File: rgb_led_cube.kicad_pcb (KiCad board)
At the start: 2 copper layers, 246.4 x 238.8 mm, 90 parts, among them Q1 IRLML6401TRPBF, Q10 MMBT2222A-TP, Q11 IRLML6401TRPBF, Q12 MMBT2222A-TP, Q13 IRLML6401TRPBF, Q14 MMBT2222A-TP, Q15 IRLML6401TRPBF, Q16 MMBT2222A-TP, Q2 MMBT2222A-TP, Q3 IRLML6401TRPBF, Q4 MMBT2222A-TP, Q5 IRLML6401TRPBF, Q6 MMBT2222A-TP, Q7 IRLML6401TRPBF, Q8 MMBT2222A-TP, Q9 IRLML6401TRPBF, U1 TLC59711PWPR, U10 TLC59711PWPR, U11 TLC59711PWPR, U12 TLC59711PWPR, U13 TLC59711PWPR, U14 TLC59711PWPR, U15 TLC59711PWPR, U16 TLC59711PWPR, U2 TLC59711PWPR, U3 TLC59711PWPR, U4 TLC59711PWPR, U5 TLC59711PWPR, U6 TLC59711PWPR, U7 TLC59711PWPR, U8 TLC59711PWPR, U9 TLC59711PWPR

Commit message: Add microphone
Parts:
- added C17: 0.1µF, Capacitor_SMD:C_0805_2012Metric_Pad1.15x1.40mm_HandSolder, F.Cu at (155.8, 70.7)
- added MK1: ICS-43434, rgb_led_cube:MIC_ICS-43434, F.Cu at (151.1, 69.6)
- added R41: 100K, Resistor_SMD:R_0805_2012Metric_Pad1.15x1.40mm_HandSolder, F.Cu at (155.8, 68.5)
- added REF1: MountingHole_3.2mm_M3, MountingHole:MountingHole_3.2mm_M3, F.Cu at (31.4, 27.4)
- added REF2: MountingHole_3.2mm_M3, MountingHole:MountingHole_3.2mm_M3, F.Cu at (269.4, 27.4)
- added REF3: MountingHole_3.2mm_M3, MountingHole:MountingHole_3.2mm_M3, F.Cu at (269.4, 265.4)
- added REF4: MountingHole_3.2mm_M3, MountingHole:MountingHole_3.2mm_M3, F.Cu at (31.4, 265.4)
- moved CNTL1 102.8 mm to (150.4, 70.3)
- moved U11 18.7 mm to (94.6, 173.8)
- moved U13 18.7 mm to (94.6, 201.7)
- moved U15 18.7 mm to (94.6, 229.6)
- moved U7 18.7 mm to (94.6, 117.9)
- moved U9 18.7 mm to (94.6, 145.8)
- moved U10 18.7 mm to (206.4, 145.8)
- moved U12 18.7 mm to (206.4, 173.8)
- moved U14 18.7 mm to (206.4, 201.7)
- moved U16 18.7 mm to (206.4, 229.6)
- moved U8 18.7 mm to (206.4, 117.9)
- moved C2 18.7 mm to (208.5, 29.3)
- moved C4 18.7 mm to (208.5, 57.2)
- moved C6 18.7 mm to (208.5, 85.1)
- moved Q1 18.7 mm to (266.0, 54.5)
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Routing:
- net Net-(CNTL1-Pad15): track 242.3 -> 138.7 mm
- net Net-(CNTL1-Pad7): track 410.9 -> 307.8 mm
- net Net-(CNTL1-Pad8): track 365.5 -> 270.8 mm
- net Net-(CNTL1-Pad12): track 265.7 -> 171.1 mm
- net Net-(CNTL1-Pad9): track 338.2 -> 244.0 mm
- net Net-(CNTL1-Pad10): track 314.7 -> 222.0 mm
- net Net-(CNTL1-Pad11): track 285.5 -> 193.2 mm
- net Net-(CNTL1-Pad13): track 235.1 -> 148.1 mm
- net Net-(CNTL1-Pad37): track 58.1 -> 125.9 mm
- net VCC: track 975.1 -> 926.0 mm, vias 25 -> 26
- net Net-(C17-Pad1): track 0.00 -> 35.2 mm, vias 0 -> 2
- net Net-(CNTL1-Pad23): track 0.00 -> 34.6 mm, vias 0 -> 2
- net Net-(CNTL1-Pad30): track 70.5 -> 101.8 mm
- net Net-(CNTL1-Pad24): track 0.00 -> 27.3 mm, vias 0 -> 2
- net Net-(CNTL1-Pad26): track 0.00 -> 17.8 mm, vias 0 -> 2
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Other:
- board size 246.4 x 238.8 mm -> 250 x 250 mm

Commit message: Improve wiring
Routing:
- net /b63: track 62.6 -> 61.6 mm, vias 1 -> 0
- net /g63: track 46.7 -> 45.8 mm, vias 1 -> 0
- net /b62: track 32.7 -> 31.9 mm, vias 1 -> 0
- net /r63: track 46.1 -> 45.3 mm, vias 1 -> 0
- net /g62: track 16.8 -> 16.1 mm, vias 1 -> 0
- net /r62: track 16.3 -> 15.7 mm, vias 1 -> 0

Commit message: Update layout
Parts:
- added J1: OSTTC022162, digikey-footprints:Term_Block_1x2_P5.08MM, F.Cu at (150.4, 40.1)
- moved C17 43.9 mm to (153.2, 114.5)
- moved R41 43.9 mm to (153.2, 112.3)
- moved MK1 43.9 mm to (148.4, 113.4)
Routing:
- net Net-(CNTL1-Pad15): track 138.7 -> 302.5 mm
- net Net-(CNTL1-Pad13): track 148.1 -> 273.1 mm
- net Net-(CNTL1-Pad12): track 171.1 -> 244.2 mm
- net Net-(C17-Pad1): track 35.2 -> 89.2 mm
- net Net-(CNTL1-Pad26): track 17.8 -> 49.9 mm
- net Net-(CNTL1-Pad23): track 34.6 -> 65.5 mm
- net Net-(CNTL1-Pad24): track 27.3 -> 58.1 mm
- net Net-(CNTL1-Pad11): track 193.2 -> 210.8 mm
- net Net-(CNTL1-Pad30): track 101.8 -> 113.0 mm
- net Net-(CNTL1-Pad37): track 125.9 -> 131.8 mm
- net Net-(CNTL1-Pad8): track 270.8 -> 266.6 mm
- net Net-(CNTL1-Pad10): track 222.0 -> 218.1 mm
- net Net-(U2-Pad11): track 152.0 -> 148.2 mm, vias 4 -> 2
- net Net-(CNTL1-Pad9): track 244.0 -> 240.5 mm
- net Net-(U12-Pad12): track 151.0 -> 154.5 mm, vias 4 -> 2
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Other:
- rule via_min_size: 0.4 -> 0.6

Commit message: PCB v2
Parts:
- moved R41 47.6 mm to (114.0, 85.3), turned to 270 degrees
- moved C17 42.7 mm to (119.1, 88.6)
- moved MK1 40.7 mm to (115.1, 90.0), turned to 0 degrees
- moved C10 14.2 mm to (208.2, 155.2)
- moved C9 14.2 mm to (96.4, 155.2)
- moved R10 14.2 mm to (204.1, 155.2)
- moved R9 14.2 mm to (92.3, 155.2)
- moved U3 14.2 mm to (94.4, 76.2)
- moved U4 14.2 mm to (206.1, 76.2)
- moved C1 14.2 mm to (96.4, 43.5)
- moved C2 14.2 mm to (208.2, 43.5)
- moved R1 14.2 mm to (92.3, 43.5)
- moved R2 14.2 mm to (204.1, 43.5)
- moved C11 14.2 mm to (96.4, 183.2)
- moved C12 14.2 mm to (208.2, 183.2)
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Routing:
- net Net-(CNTL1-Pad15): track 302.5 -> 134.6 mm, vias 2 -> 0
- net Net-(CNTL1-Pad13): track 273.1 -> 132.2 mm, vias 2 -> 0
- net VCC: track 928.4 -> 1064.7 mm
- net Net-(CNTL1-Pad12): track 244.2 -> 160.1 mm, vias 2 -> 0
- net Net-(CNTL1-Pad23): track 65.5 -> 30.4 mm, vias 2 -> 0
- net Net-(CNTL1-Pad11): track 210.8 -> 181.3 mm, vias 2 -> 0
- net Net-(CNTL1-Pad24): track 58.1 -> 35.3 mm, vias 2 -> 0
- net /b57: track 21.7 -> 3.86 mm
- net /b9: track 21.7 -> 3.86 mm
- net /b17: track 21.7 -> 3.86 mm
- net /b49: track 21.7 -> 3.86 mm
- net /b25: track 21.7 -> 3.86 mm
- net /b41: track 21.7 -> 3.86 mm
- net /b33: track 21.7 -> 3.86 mm
- net /b1: track 21.3 -> 3.86 mm
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
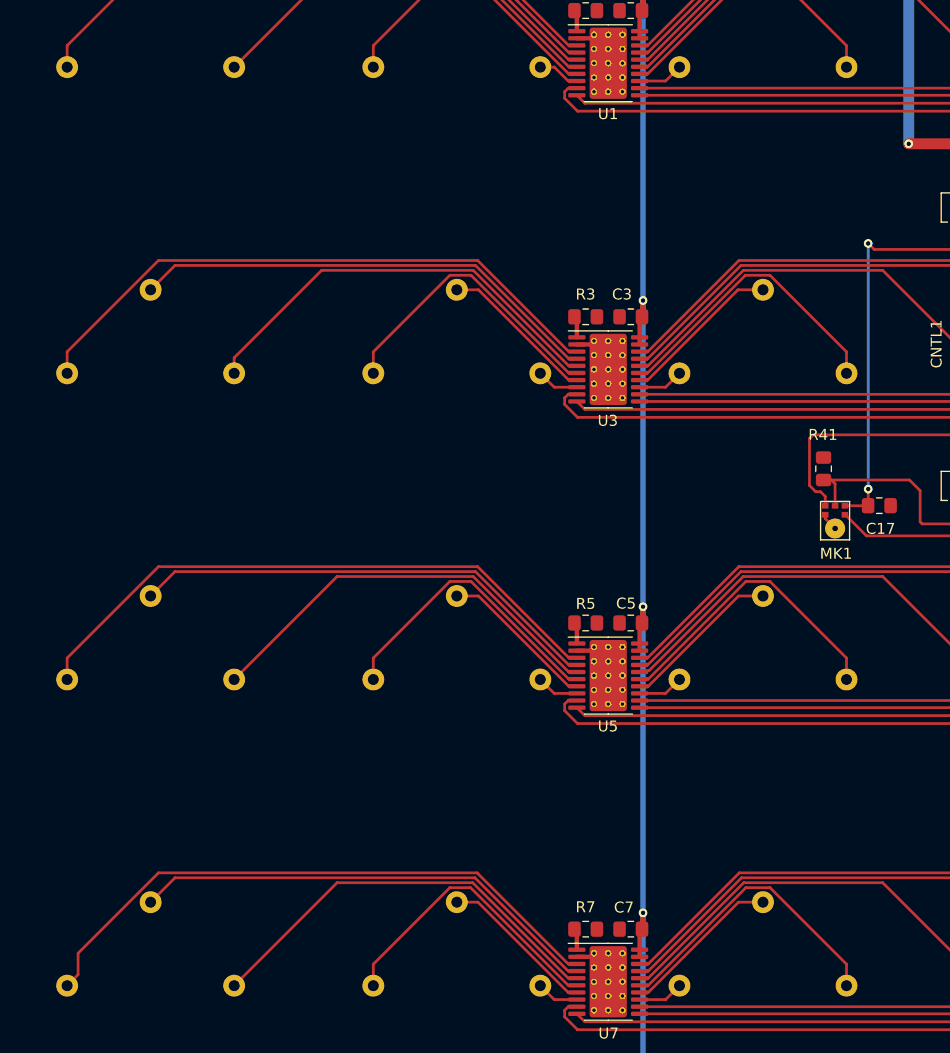
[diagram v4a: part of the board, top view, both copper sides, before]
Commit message: Align tracks
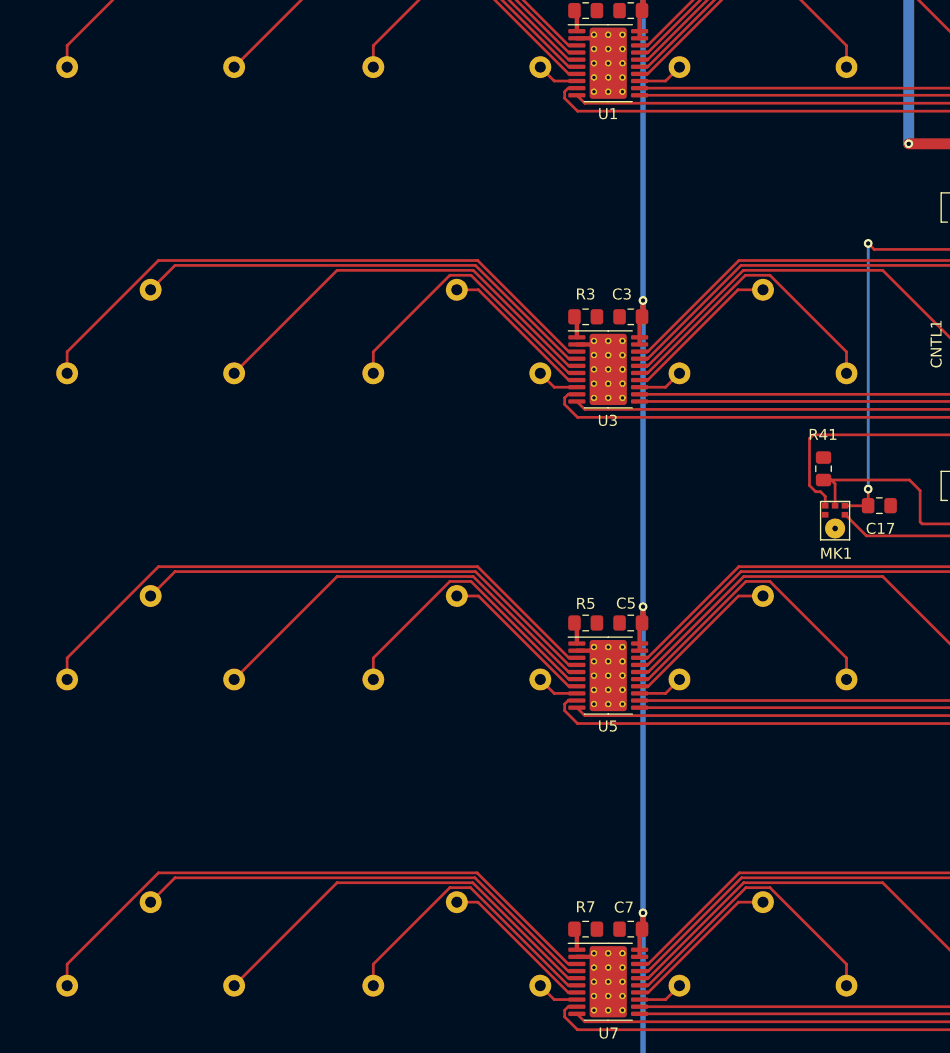
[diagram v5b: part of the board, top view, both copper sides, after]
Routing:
- net GND: track 28.8 -> 27.2 mm
- net /b8: track 39.6 -> 38.8 mm

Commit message: Add Mounting holes
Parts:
- H1: renamed from REF1; value MountingHole_3.2mm_M3 -> MountingHole_Pad; footprint MountingHole:MountingHole_3.2mm_M3 -> MountingHole:MountingHole_3.2mm_M3_Pad_Via
- H2: renamed from REF2; value MountingHole_3.2mm_M3 -> MountingHole_Pad; footprint MountingHole:MountingHole_3.2mm_M3 -> MountingHole:MountingHole_3.2mm_M3_Pad_Via
- H3: renamed from REF4; value MountingHole_3.2mm_M3 -> MountingHole_Pad; footprint MountingHole:MountingHole_3.2mm_M3 -> MountingHole:MountingHole_3.2mm_M3_Pad_Via
- H4: renamed from REF3; value MountingHole_3.2mm_M3 -> MountingHole_Pad; footprint MountingHole:MountingHole_3.2mm_M3 -> MountingHole:MountingHole_3.2mm_M3_Pad_Via
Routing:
- net GND: vias 0 -> 2
- added copper zone on B.Cu, net GND
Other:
- board text added: "+5V"
- board text added: "GND"
- board text added: "JLCJLCJLCJLC"
